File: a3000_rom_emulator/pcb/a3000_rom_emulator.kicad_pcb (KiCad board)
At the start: 4 copper layers, 43.2 x 78.7 mm, 81 parts

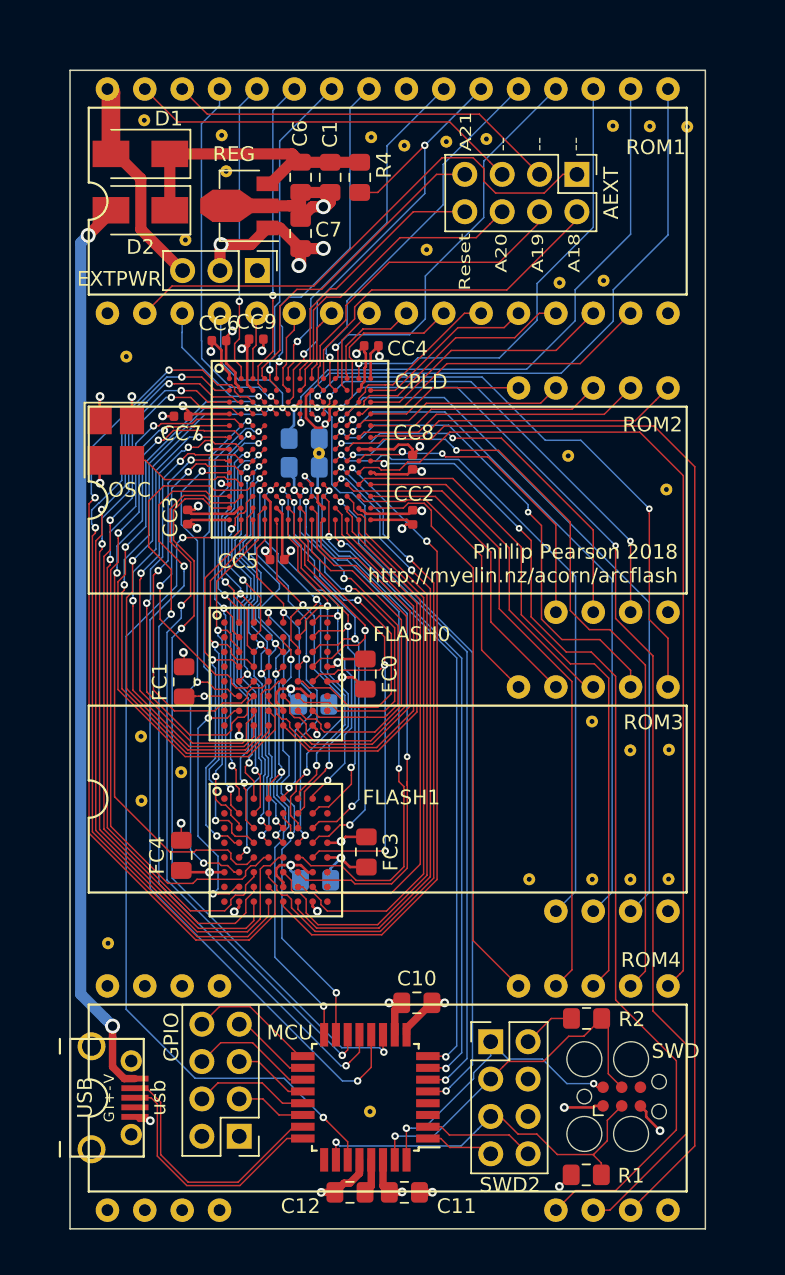
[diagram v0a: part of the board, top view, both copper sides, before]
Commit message: Added AEXT2 connector to bring A18:21 out at a second location that is more convenient on A310/A3000
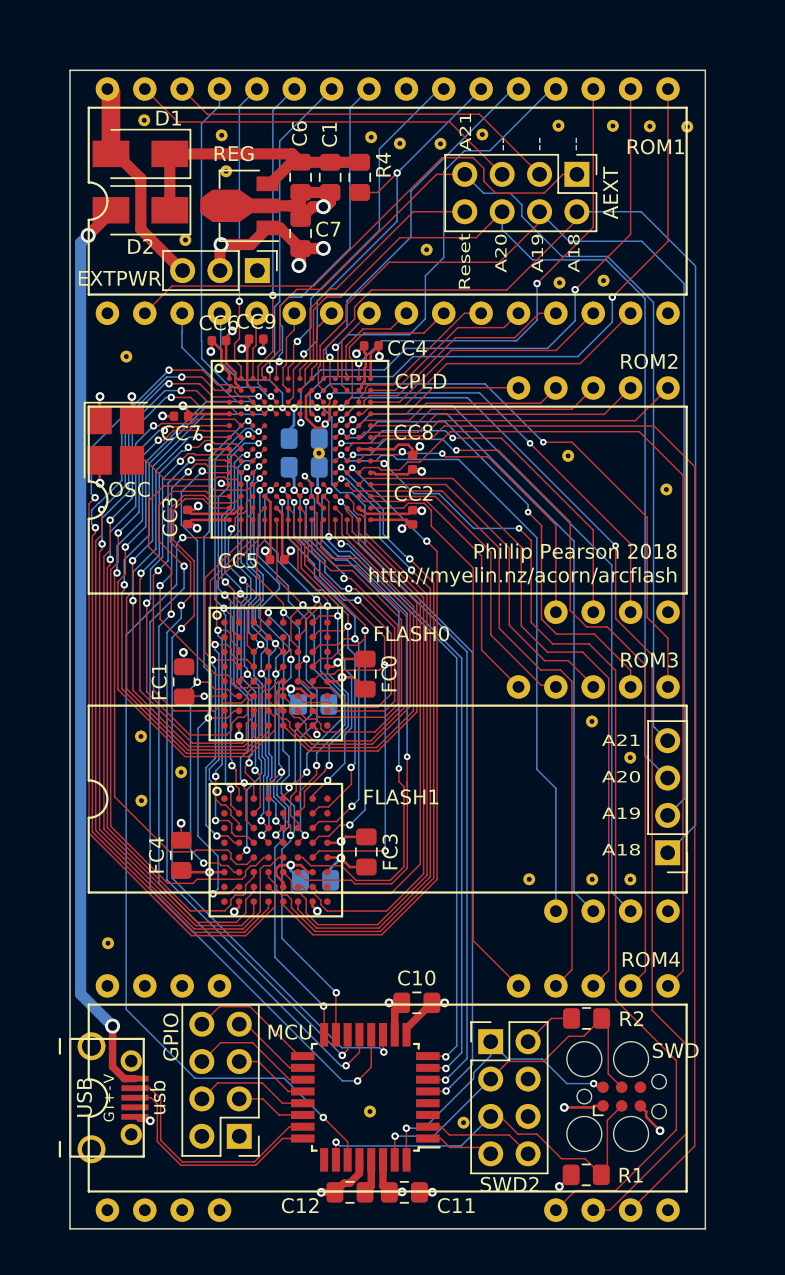
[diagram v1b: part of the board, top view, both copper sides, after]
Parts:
- added AEXT2: Addresses, Connector_PinHeader_2.54mm:PinHeader_1x04_P2.54mm_Vertical, F.Cu at (180.3, 82.4)
- moved staple_single6 43.1 mm to (172.9, 33.0)
- moved staple_single7 21.6 mm to (166.4, 100.7)
- moved staple_single5 0.50 mm to (177.8, 75.9)
- moved staple_single18 0.42 mm to (164.9, 34.2)
- moved staple_single1 0.41 mm to (167.7, 33.6)
- moved staple_single17 0.33 mm to (162.1, 34.2)
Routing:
- net rom_A16: track 23.9 -> 74.1 mm
- net rom_A17: track 22.9 -> 71.4 mm
- net rom_A19: track 21.8 -> 68.8 mm
- net rom_A18: track 21.4 -> 67.5 mm
- net rom_nCS: track 32.5 -> 29.8 mm
- net USBDP: track 17.3 -> 15.6 mm
- net USBDM: track 17.7 -> 16.1 mm
- net rom_D18: track 49.4 -> 47.9 mm
- net rom_D6: track 28.5 -> 29.6 mm
- net rom_D17: track 46.5 -> 45.4 mm
- net rom_D16: track 43.5 -> 42.4 mm
- net rom_D19: track 40.0 -> 39.2 mm
- net rom_D30: track 44.4 -> 45.2 mm
- net rom_D10: track 31.6 -> 30.8 mm
- net mcu_RESET: track 26.4 -> 27.1 mm
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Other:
- board text added: "A21 A20 A19 A18"

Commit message: Added some more staples
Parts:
- added staple_single31: , myelin-kicad:via_single, F.Cu at (177.9, 88.2)
- added staple_single32: , myelin-kicad:via_single, F.Cu at (180.4, 88.1)
- added staple_single33: , myelin-kicad:via_single, F.Cu at (165.9, 65.9)
- moved staple_single13 1.10 mm to (179.1, 34.1)
- moved staple_single14 1.06 mm to (181.6, 34.1)
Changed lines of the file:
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@@
     (thickness 1.6)
     (drawings 11)
-    (tracks 2461)
+    (tracks 2459)
     (zones 0)
-    (modules 82)
+    (modules 85)
     (nets 147)
   )
@@
   (module myelin-kicad:dip32_rom (layer F.Cu)
     (at 170.18 38.1)
-    (fp_text reference ROM1 (at 9.3345 -3.6576) (layer F.SilkS)
+    (fp_text reference ROM1 (at 9.07034 -5.30098) (layer F.SilkS)
       (effects (font (size 1 1) (thickness 0.15)))
     )
@@
     (tags "Diode SMA (DO-214AC)")
     (attr smd)
-    (fp_text reference D1 (at -1.92052 2.39832 180) (layer F.SilkS)
+    (fp_text reference D1 (at 1.21384 2.36276 180) (layer F.SilkS)
       (effects (font (size 1 1) (thickness 0.15)))
     )
@@
     (tags "Diode SMA (DO-214AC)")
     (attr smd)
-    (fp_text reference D2 (at 0 -2.5 180) (layer F.SilkS)
+    (fp_text reference D2 (at 1.24686 -2.48642 180) (layer F.SilkS)
       (effects (font (size 1 1) (thickness 0.15)))
     )
@@
   )
   (module myelin-kicad:via_single (layer F.Cu)
-    (at 179.10556 33.01492)
+    (at 179.11572 34.11982)
     (descr "Via array for stapling planes together")
     (fp_text reference staple_single13 (at 0 -1) (layer F.SilkS) hide
@@
   )
   (module myelin-kicad:via_single (layer F.Cu)
-    (at 181.6481 33.04286)
+    (at 181.63794 34.10712)
     (descr "Via array for stapling planes together")
     (fp_text reference staple_single14 (at 0 -1) (layer F.SilkS) hide
@@
     )
   )
+  (module myelin-kicad:via_single (layer F.Cu)
+    (at 177.92954 88.20912)
+    (descr "Via array for stapling planes together")
+    (fp_text reference staple_single31 (at 0 -1) (layer F.SilkS) hide
+      (effects (font (size 1 1) (thickness 0.15)))
+    )
+    (fp_text value "" (at 0 1) (layer F.SilkS) hide
+      (effects (font (size 1 1) (thickness 0.15)))
+    )
+    (pad 1 thru_hole circle (at 0 0) (size 0.8128 0.8128) (drill 0.3302) (layers *.Cu)
+      (net 27 GND) (zone_connect 2))
+  )
+  (module myelin-kicad:via_single (layer F.Cu)
+    (at 180.38572 88.12276)
+    (descr "Via array for stapling planes together")
+    (fp_text reference staple_single32 (at 0 -1) (layer F.SilkS) hide
+      (effects (font (size 1 1) (thickness 0.15)))
+    )
+    (fp_text value "" (at 0 1) (layer F.SilkS) hide
+      (effects (font (size 1 1) (thickness 0.15)))
+    )
+    (pad 1 thru_hole circle (at 0 0) (size 0.8128 0.8128) (drill 0.3302) (layers *.Cu)
+      (net 27 GND) (zone_connect 2))
+  )
+  (module myelin-kicad:via_single (layer F.Cu)
+    (at 165.91534 65.9003)
+    (descr "Via array for stapling planes together")
+    (fp_text reference staple_single33 (at 0 -1) (layer F.SilkS) hide
+      (effects (font (size 1 1) (thickness 0.15)))
+    )
+    (fp_text value "" (at 0 1) (layer F.SilkS) hide
+      (effects (font (size 1 1) (thickness 0.15)))
+    )
+    (pad 1 thru_hole circle (at 0 0) (size 0.8128 0.8128) (drill 0.3302) (layers *.Cu)
+      (net 27 GND) (zone_connect 2))
+  )
   (gr_text "A21\n\nA20\n\nA19\n\nA18" (at 178.53152 78.49362) (layer F.SilkS)
     (effects (font (size 0.77 1) (thickness 0.1)) (justify right))
@@
   (segment (start 162.594169 77.639998) (end 162.594167 77.64) (width 0.1016) (layer F.Cu) (net 54))
   (segment (start 162.6108 75.86472) (end 162.6108 77.568676) (width 0.1016) (layer F.Cu) (net 54))
-  (segment (start 162.6108 66.1289) (end 162.6108 75.86472) (width 0.1016) (layer B.Cu) (net 54))
-  (segment (start 158.71444 62.23254) (end 162.6108 66.1289) (width 0.1016) (layer B.Cu) (net 54))
-  (segment (start 157.90418 62.23254) (end 158.71444 62.23254) (width 0.1016) (layer B.Cu) (net 54))
+  (segment (start 162.6108 66.54546) (end 162.6108 75.86472) (width 0.1016) (layer B.Cu) (net 54))
+  (segment (start 157.32 57.78) (end 156.83 58.27) (width 0.1016) (layer B.Cu) (net 54))
+  (segment (start 158.29788 62.23254) (end 162.6108 66.54546) (width 0.1016) (layer B.Cu) (net 54))
   (segment (start 156.83 61.15836) (end 157.90418 62.23254) (width 0.1016) (layer B.Cu) (net 54))
+  (segment (start 157.90418 62.23254) (end 158.29788 62.23254) (width 0.1016) (layer B.Cu) (net 54))
   (segment (start 156.83 58.27) (end 156.83 61.15836) (width 0.1016) (layer B.Cu) (net 54))
-  (segment (start 157.32 57.78) (end 156.83 58.27) (width 0.1016) (layer B.Cu) (net 54))
   (segment (start 154.19 83.71) (end 154.750299 84.270299) (width 0.1016) (layer F.Cu) (net 55))
   (segment (start 159.777199 60.658055) (end 159.777199 59.685053) (width 0.1016) (layer F.Cu) (net 55))
@@
   (segment (start 162.04946 77.549459) (end 162.39 77.889999) (width 0.1016) (layer F.Cu) (net 58))
   (segment (start 162.04946 76.65974) (end 162.04946 77.549459) (width 0.1016) (layer F.Cu) (net 58))
-  (segment (start 162.04946 66.0019) (end 162.04946 76.65974) (width 0.1016) (layer B.Cu) (net 58))
-  (segment (start 158.54426 62.4967) (end 162.04946 66.0019) (width 0.1016) (layer B.Cu) (net 58))
+  (segment (start 162.04946 66.39052) (end 162.04946 76.65974) (width 0.1016) (layer B.Cu) (net 58))
+  (segment (start 158.15564 62.4967) (end 162.04946 66.39052) (width 0.1016) (layer B.Cu) (net 58))
+  (segment (start 157.75432 62.4967) (end 158.15564 62.4967) (width 0.1016) (layer B.Cu) (net 58))
   (segment (start 156.31668 61.05906) (end 157.75432 62.4967) (width 0.1016) (layer B.Cu) (net 58))
   (segment (start 156.31668 58.33364) (end 156.31668 61.05906) (width 0.1016) (layer B.Cu) (net 58))
-  (segment (start 156.097198 57.227198) (end 156.097198 58.114158) (width 0.1016) (layer B.Cu) (net 58))
-  (segment (start 157.75432 62.4967) (end 158.54426 62.4967) (width 0.1016) (layer B.Cu) (net 58))
   (segment (start 156.097198 58.114158) (end 156.31668 58.33364) (width 0.1016) (layer B.Cu) (net 58))
+  (segment (start 156.097198 57.227198) (end 156.097198 58.114158) (width 0.1016) (layer B.Cu) (net 58))
   (segment (start 155.66 56.79) (end 156.097198 57.227198) (width 0.1016) (layer B.Cu) (net 58))
   (via (at 146.4321 50.51255) (size 0.51) (drill 0.25) (layers F.Cu B.Cu) (net 59))
@@
   (segment (start 165.23 98.61) (end 165.26 98.58) (width 0.1016) (layer F.Cu) (net 116))
   (segment (start 164.02 98.61) (end 165.23 98.61) (width 0.1016) (layer F.Cu) (net 116))
-  (segment (start 156.860624 52.14) (end 157.492801 52.772177) (width 0.1016) (layer B.Cu) (net 116))
-  (segment (start 167.05 68.770088) (end 167.05 96.79) (width 0.1016) (layer B.Cu) (net 116))
-  (segment (start 159.74 58.800546) (end 159.74 61.460088) (width 0.1016) (layer B.Cu) (net 116))
-  (segment (start 165.514999 98.325001) (end 165.26 98.58) (width 0.1016) (layer B.Cu) (net 116))
-  (segment (start 157.492801 57.356655) (end 158.046692 57.910546) (width 0.1016) (layer B.Cu) (net 116))
-  (segment (start 158.046692 57.910546) (end 158.85 57.910546) (width 0.1016) (layer B.Cu) (net 116))
-  (segment (start 158.85 57.910546) (end 159.74 58.800546) (width 0.1016) (layer B.Cu) (net 116))
-  (segment (start 157.492801 52.772177) (end 157.492801 57.356655) (width 0.1016) (layer B.Cu) (net 116))
   (segment (start 167.05 96.79) (end 165.514999 98.325001) (width 0.1016) (layer B.Cu) (net 116))
+  (segment (start 167.05 68.32782) (end 167.05 96.79) (width 0.1016) (layer B.Cu) (net 116))
+  (segment (start 160.24352 61.52134) (end 167.05 68.32782) (width 0.1016) (layer B.Cu) (net 116))
+  (segment (start 160.24352 59.74588) (end 160.24352 61.52134) (width 0.1016) (layer B.Cu) (net 116))
+  (segment (start 157.492801 52.772177) (end 157.492801 56.995161) (width 0.1016) (layer B.Cu) (net 116))
+  (segment (start 165.514999 98.325001) (end 165.26 98.58) (width 0.1016) (layer B.Cu) (net 116))
+  (segment (start 157.492801 56.995161) (end 160.24352 59.74588) (width 0.1016) (layer B.Cu) (net 116))
+  (segment (start 156.860624 52.14) (end 157.492801 52.772177) (width 0.1016) (layer B.Cu) (net 116))
   (segment (start 156.5 52.14) (end 156.860624 52.14) (width 0.1016) (layer B.Cu) (net 116))
-  (segment (start 159.74 61.460088) (end 167.05 68.770088) (width 0.1016) (layer B.Cu) (net 116))
   (segment (start 165.21 97.01) (end 165.25 97.05) (width 0.1016) (layer F.Cu) (net 117))
   (via (at 165.25 97.05) (size 0.51) (drill 0.25) (layers F.Cu B.Cu) (net 117))

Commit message: Updated URL
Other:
- board text added: "Phillip Pearson 2018 http://myelin.nz/arcflash"
- board text added: "http://myelin.nz/arcflash by Phillip Pearson, pp@myelin.nz Copyright 2018 Google LLC"
- board text removed: "Phillip Pearson 2018 http://myelin.nz/acorn/arcflash"
- board text removed: "http://myelin.nz/acorn/arcflash by Phillip Pearson, pp@myelin.nz Copyright 2018 Google LLC"
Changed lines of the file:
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@@
     (34 B.Paste user)
     (35 F.Paste user)
-    (36 B.SilkS user hide)
+    (36 B.SilkS user)
     (37 F.SilkS user)
     (38 B.Mask user)
@@
     (effects (font (size 5.08 5.08) (thickness 1.27) italic) (justify mirror))
   )
-  (gr_text "http://myelin.nz/acorn/arcflash\nby Phillip Pearson, pp@myelin.nz\nCopyright 2018 Google LLC" (at 164.16 68.3 90) (layer B.SilkS)
+  (gr_text "http://myelin.nz/arcflash\nby Phillip Pearson, pp@myelin.nz\nCopyright 2018 Google LLC" (at 164.16 68.3 90) (layer B.SilkS)
     (effects (font (size 1 1) (thickness 0.1778)) (justify mirror))
   )
-  (gr_text "Phillip Pearson 2018\nhttp://myelin.nz/acorn/arcflash" (at 181.02072 62.74562) (layer F.SilkS)
+  (gr_text "Phillip Pearson 2018\nhttp://myelin.nz/arcflash" (at 181.02072 62.74562) (layer F.SilkS)
     (effects (font (size 1 1) (thickness 0.1778)) (justify right))
   )

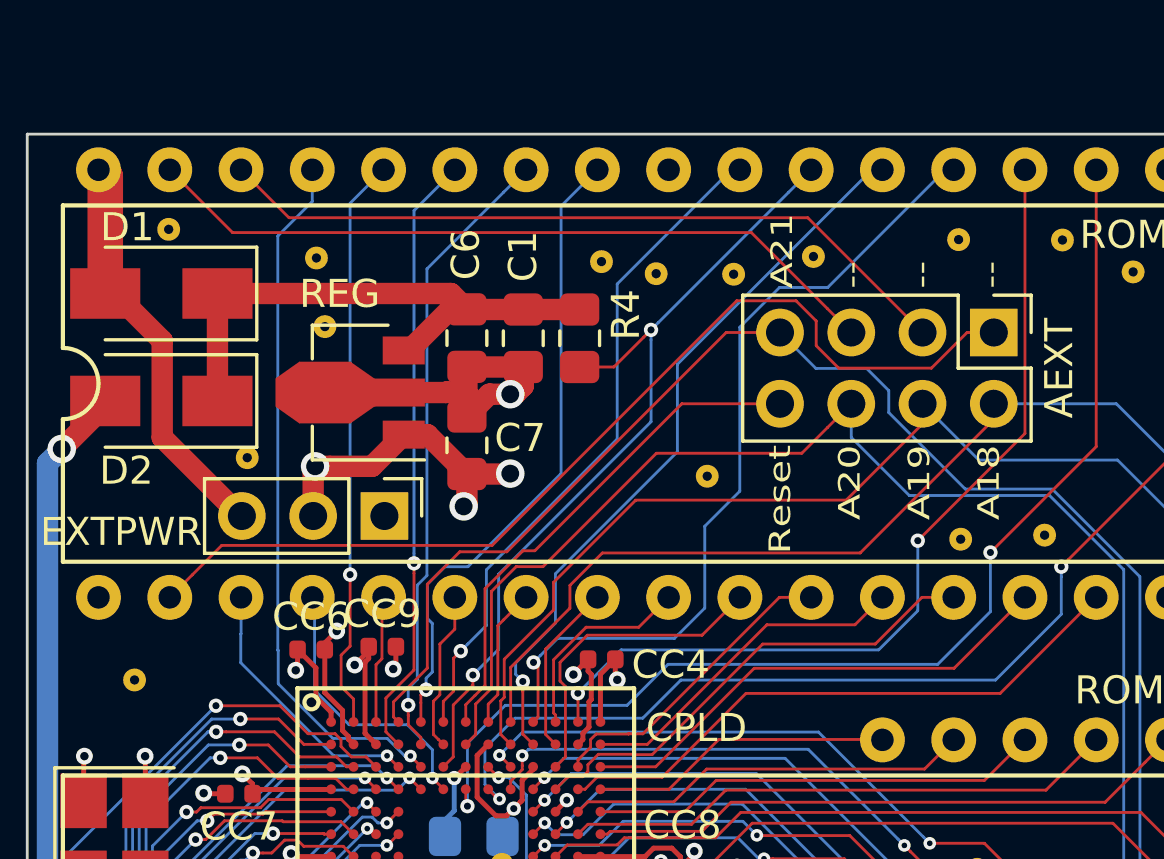
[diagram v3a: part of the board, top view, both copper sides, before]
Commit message: Added pullup on A21, for predictable results when it's not wired to the motherboard
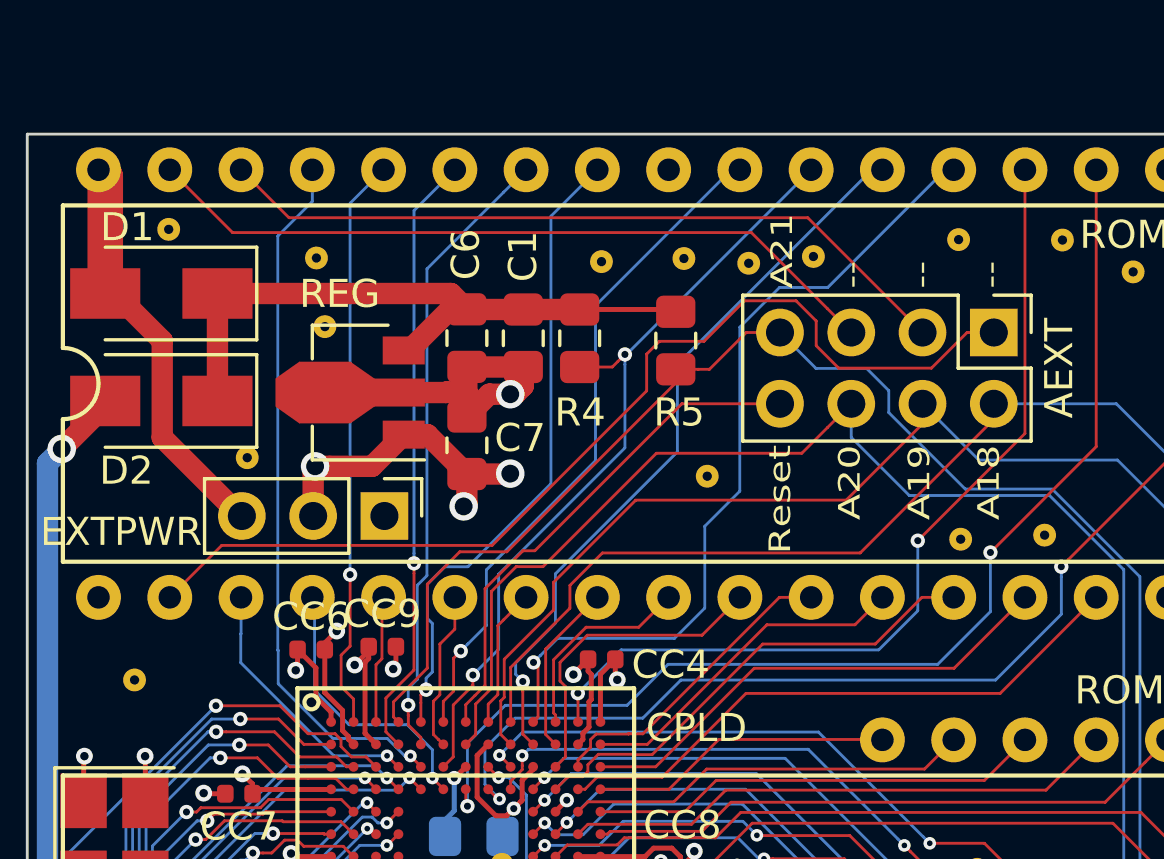
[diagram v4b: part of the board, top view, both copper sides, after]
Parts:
- added R5: 10k, Resistor_SMD:R_0805_2012Metric_Pad1.15x1.40mm_HandSolder, F.Cu at (162.8, 36.6)
- moved staple_single17 1.13 mm to (163.1, 33.6)
- moved staple_single18 0.66 mm to (165.4, 33.8)
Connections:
- USB pad 4: USB_ID -> (no net)
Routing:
- net 5V: track 19.8 -> 23.3 mm
- net rom_nCS: track 29.8 -> 28.5 mm
- net rom_A16_ext: track 35.8 -> 36.6 mm
